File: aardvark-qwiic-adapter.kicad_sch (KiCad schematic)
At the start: 7 parts, among them J1 Conn_02x05_Odd_Even, J2 Conn_01x04, J3 Conn_01x04, J4 Conn_01x02, U1 AP7361C-33E

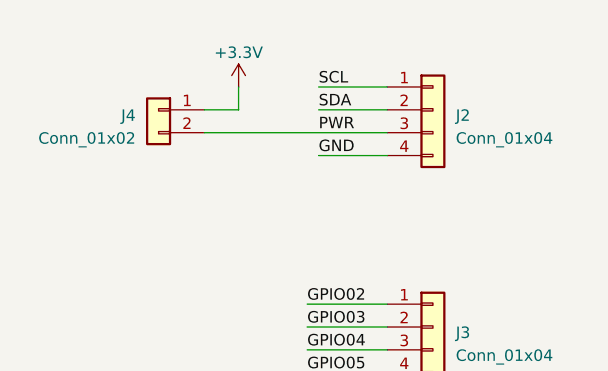
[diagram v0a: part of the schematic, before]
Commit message: Fix backwards QWIIC
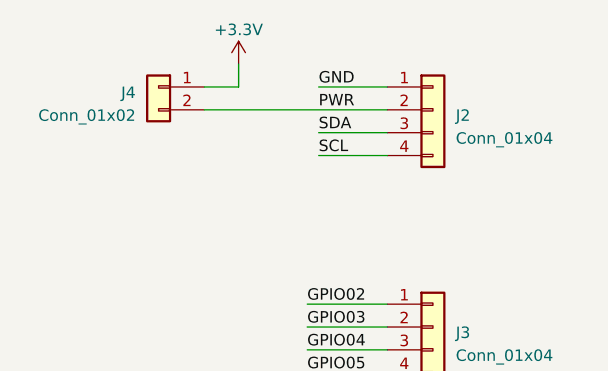
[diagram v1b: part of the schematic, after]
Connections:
- net GND: now also J2.1 (Pin_1); no longer J2.4 (Pin_4)
- net PWR: now also J2.2 (Pin_2); no longer J2.3 (Pin_3)
- net SCL: now also J2.4 (Pin_4); no longer J2.1 (Pin_1)
- net SDA: now also J2.3 (Pin_3); no longer J2.2 (Pin_2)
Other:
- moved on the sheet: J4
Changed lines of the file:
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@@
   (title_block
     (title "Aardvark QWIIC Adapter")
-    (date "2023-02-19")
-    (rev "1.0")
+    (date "2023-02-22")
+    (rev "1.1")
   )
   (junction (at 151.13 93.98) (diameter 0) (color 0 0 0 0)
@@
     (stroke (width 0) (type default))
   )
+  (wire (pts (xy 83.82 96.52) (xy 91.44 96.52))
+    (stroke (width 0) (type default))
+  )
   (wire (pts (xy 195.58 93.98) (xy 199.39 93.98))
     (stroke (width 0) (type default))
@@
     (stroke (width 0) (type default))
   )
-  (wire (pts (xy 74.93 93.98) (xy 71.12 93.98))
+  (wire (pts (xy 74.93 91.44) (xy 71.12 91.44))
     (stroke (width 0) (type default))
   )
@@
     (stroke (width 0) (type default))
   )
-  (wire (pts (xy 83.82 93.98) (xy 91.44 93.98))
+  (wire (pts (xy 71.12 93.98) (xy 91.44 93.98))
     (stroke (width 0) (type default))
   )
@@
     (stroke (width 0) (type default))
   )
-  (wire (pts (xy 71.12 96.52) (xy 91.44 96.52))
-    (stroke (width 0) (type default))
-  )
   (wire (pts (xy 173.99 104.14) (xy 173.99 105.41))
     (stroke (width 0) (type default))
@@
     (stroke (width 0) (type default))
   )
-  (wire (pts (xy 74.93 91.44) (xy 74.93 93.98))
+  (wire (pts (xy 74.93 88.9) (xy 74.93 91.44))
     (stroke (width 0) (type default))
   )
   (label "GPIO05" (at 129.54 101.6 0) (fields_autoplaced)
+    (effects (font (size 1.27 1.27)) (justify left bottom))
+  )
+  (label "SDA" (at 83.82 96.52 0) (fields_autoplaced)
     (effects (font (size 1.27 1.27)) (justify left bottom))
   )
@@
     (effects (font (size 1.27 1.27)) (justify left bottom))
   )
-  (label "PWR" (at 83.82 96.52 0) (fields_autoplaced)
-    (effects (font (size 1.27 1.27)) (justify left bottom))
-  )
   (label "GPIO02" (at 82.55 115.57 0) (fields_autoplaced)
     (effects (font (size 1.27 1.27)) (justify left bottom))
@@
     (effects (font (size 1.27 1.27)) (justify right bottom))
   )
-  (label "GND" (at 83.82 99.06 0) (fields_autoplaced)
-    (effects (font (size 1.27 1.27)) (justify left bottom))
-  )
-  (label "SDA" (at 83.82 93.98 0) (fields_autoplaced)
-    (effects (font (size 1.27 1.27)) (justify left bottom))
-  )
-  (label "SCL" (at 83.82 91.44 0) (fields_autoplaced)
+  (label "SCL" (at 83.82 99.06 0) (fields_autoplaced)
+    (effects (font (size 1.27 1.27)) (justify left bottom))
+  )
+  (label "PWR" (at 83.82 93.98 0) (fields_autoplaced)
+    (effects (font (size 1.27 1.27)) (justify left bottom))
+  )
+  (label "GND" (at 83.82 91.44 0) (fields_autoplaced)
     (effects (font (size 1.27 1.27)) (justify left bottom))
   )
@@
     )
   )
-  (symbol (lib_id "Connector_Generic:Conn_01x02") (at 66.04 93.98 0) (mirror y) (unit 1)
+  (symbol (lib_id "Connector_Generic:Conn_01x02") (at 66.04 91.44 0) (mirror y) (unit 1)
     (in_bom yes) (on_board yes) (dnp no)
-    (property "Reference" "J4" (at 63.5 94.615 0)
+    (property "Reference" "J4" (at 63.5 92.075 0)
       (effects (font (size 1.27 1.27)) (justify left))
     )
-    (property "Value" "Conn_01x02" (at 63.5 97.155 0)
+    (property "Value" "Conn_01x02" (at 63.5 94.615 0)
       (effects (font (size 1.27 1.27)) (justify left))
     )
-    (property "Footprint" "Connector_PinHeader_2.54mm:PinHeader_1x02_P2.54mm_Vertical" (at 66.04 93.98 0)
-      (effects (font (size 1.27 1.27)) hide)
-    )
-    (property "Datasheet" "~" (at 66.04 93.98 0)
+    (property "Footprint" "Connector_PinHeader_2.54mm:PinHeader_1x02_P2.54mm_Vertical" (at 66.04 91.44 0)
+      (effects (font (size 1.27 1.27)) hide)
+    )
+    (property "Datasheet" "~" (at 66.04 91.44 0)
       (effects (font (size 1.27 1.27)) hide)
     )
@@
     )
   )
-  (symbol (lib_id "power:+3.3V") (at 74.93 91.44 0) (unit 1)
+  (symbol (lib_id "power:+3.3V") (at 74.93 88.9 0) (unit 1)
     (in_bom yes) (on_board yes) (dnp no) (fields_autoplaced)
-    (property "Reference" "#PWR05" (at 74.93 95.25 0)
-      (effects (font (size 1.27 1.27)) hide)
-    )
-    (property "Value" "+3.3V" (at 74.93 87.63 0)
+    (property "Reference" "#PWR05" (at 74.93 92.71 0)
+      (effects (font (size 1.27 1.27)) hide)
+    )
+    (property "Value" "+3.3V" (at 74.93 85.09 0)
       (effects (font (size 1.27 1.27)))
     )
-    (property "Footprint" "" (at 74.93 91.44 0)
-      (effects (font (size 1.27 1.27)) hide)
-    )
-    (property "Datasheet" "" (at 74.93 91.44 0)
-      (effects (font (size 1.27 1.27)) hide)
-    )
+    (property "Footprint" "" (at 74.93 88.9 0)
+      (effects (font (size 1.27 1.27)) hide)
+    )
+    (property "Datasheet" "" (at 74.93 88.9 0)
+      (effects (font (size 1.27 1.27)) hide)
+    )
